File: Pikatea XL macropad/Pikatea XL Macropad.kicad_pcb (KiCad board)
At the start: 2 copper layers, 140.7 x 41 mm, 40 parts, among them J1 TC2030-CTX, J2 USB_B_Mini, J3 Conn_01x03_Male, J7 Conn_01x03_Male, SW1 SW_DPST, SW2 Rotary_Encoder_Switch, SW3 Rotary_Encoder_Switch, U1 ATMEGA32U4-EP, X1 16MHz

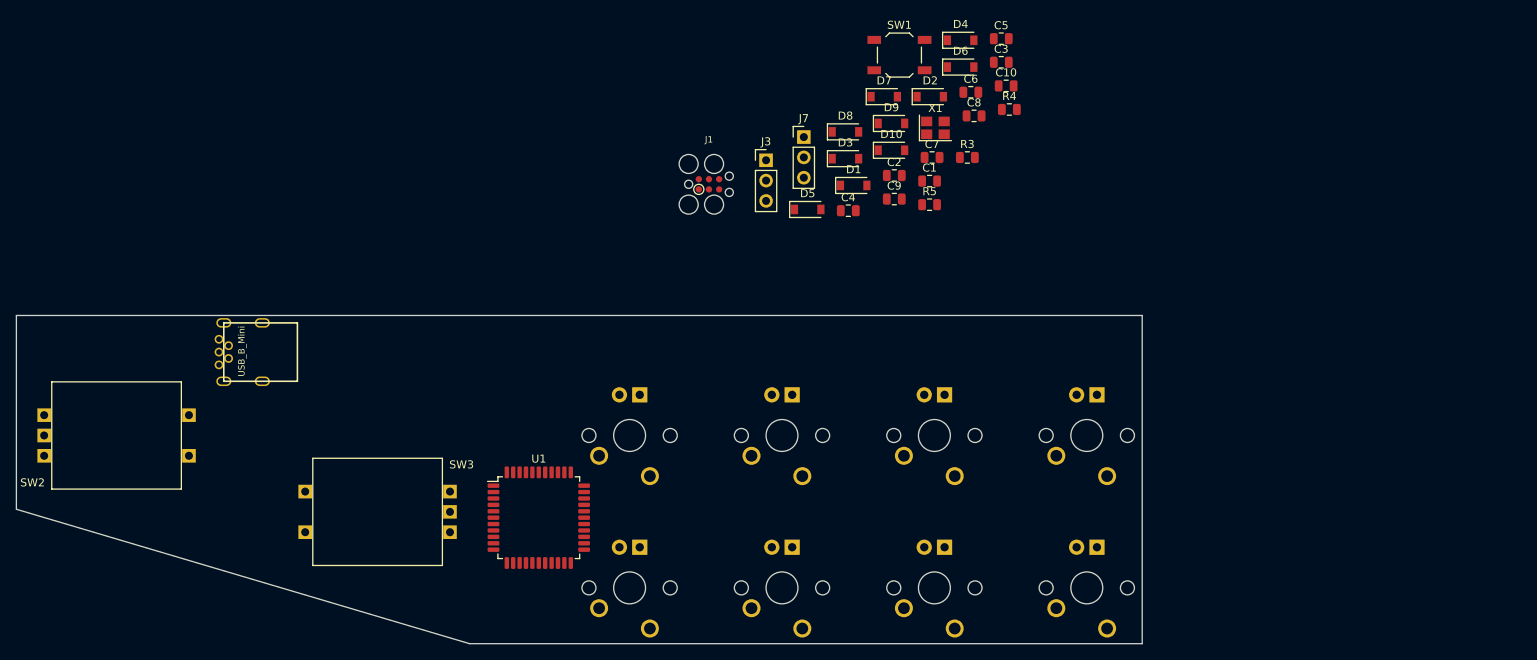
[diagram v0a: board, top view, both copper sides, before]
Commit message: add xl macropad pcb
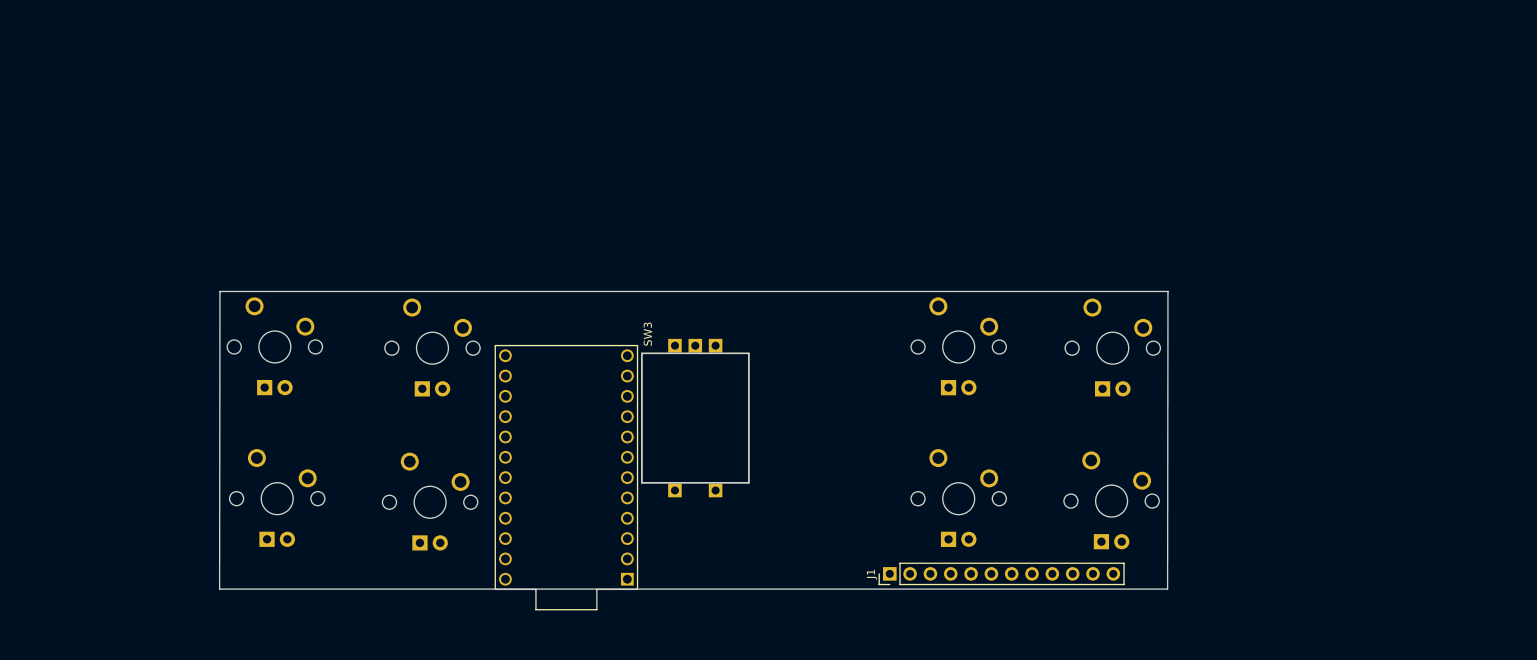
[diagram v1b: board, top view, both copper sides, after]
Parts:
- removed C1, C10, C2, C3, C4, C5: 0u1, Capacitor_SMD:C_0805_2012Metric
- removed C6: 4u7, Capacitor_SMD:C_0805_2012Metric
- removed C7, C8: 22p, Capacitor_SMD:C_0805_2012Metric
- removed C9: 1u, Capacitor_SMD:C_0805_2012Metric
- removed D1, D10, D2, D3, D4, D5, D6, D7, D8, D9: 1N4148W, Diode_SMD:D_SOD-123
- removed J2: USB_B_Mini, usb_mini:USB-Mini-B_ LCSC-C46398
- removed J3, J7: Conn_01x03_Male, Connector_PinHeader_2.54mm:PinHeader_1x03_P2.54mm_Vertical
- removed R3: 10K, Resistor_SMD:R_0805_2012Metric
- removed R4, R5: 22, Resistor_SMD:R_0805_2012Metric
- removed SW1: SW_DPST, Button_Switch_SMD:SW_SPST_TL3342
- removed SW2: Rotary_Encoder_Switch, Pikatea Macropad Encoder Side Mount:Encoder-BI_EN11_HSM0E
- removed X1: 16MHz, Crystal:Crystal_SMD_SeikoEpson_FA238-4Pin_3.2x2.5mm
- J1: value TC2030-CTX -> Conn_01x12_Female; footprint TC2030-CTX:TC2030-IDC -> Connector_PinHeader_2.54mm:PinHeader_1x12_P2.54mm_Vertical
- U1: value ATMEGA32U4-EP -> ProMicro; footprint Package_QFP:LQFP-44_10x10mm_P0.8mm -> promicro:ProMicro
- moved J1 53.7 mm to (132.5, 117.3), turned to 90 degrees
- moved MX1 45.7 mm to (55.7, 88.9), turned to 180 degrees
- moved MX5 45.4 mm to (56.0, 107.9), turned to 180 degrees
- moved MX6 45.3 mm to (75.1, 108.3), turned to 180 degrees
- moved MX2 45.0 mm to (75.4, 89.1), turned to 180 degrees
- moved SW3 41.4 mm to (108.2, 97.8), turned to 270 degrees
- moved MX7 11.6 mm to (141.1, 107.9), turned to 180 degrees
- moved MX3 11.5 mm to (141.1, 88.9), turned to 180 degrees
- moved MX4 11.4 mm to (160.4, 89.1), turned to 180 degrees
- moved MX8 11.3 mm to (160.2, 108.2), turned to 180 degrees
- moved U1 7.16 mm to (92.1, 104.0), turned to 90 degrees
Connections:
- J1 pad 1: VBUS -> (no net)
- J1 pad 2: /MOSI -> (no net)
- J1 pad 3: /RESET -> (no net)
- J1 pad 4: /SCK -> (no net)
- J1 pad 5: GND -> (no net)
- J1 pad 6: /MISO -> (no net)
- MX1 pad 3: Net-(MX1-Pad3) -> (no net)
- MX1 pad 4: Net-(MX1-Pad4) -> (no net)
- MX2 pad 3: Net-(MX2-Pad3) -> (no net)
- MX2 pad 4: Net-(MX2-Pad4) -> (no net)
- MX3 pad 3: Net-(MX3-Pad3) -> (no net)
- MX3 pad 4: Net-(MX3-Pad4) -> (no net)
- MX4 pad 3: Net-(MX4-Pad3) -> (no net)
- MX4 pad 4: Net-(MX4-Pad4) -> (no net)
- MX5 pad 3: Net-(MX5-Pad3) -> (no net)
- MX5 pad 4: Net-(MX5-Pad4) -> (no net)
- MX6 pad 3: Net-(MX6-Pad3) -> (no net)
- MX6 pad 4: Net-(MX6-Pad4) -> (no net)
- MX7 pad 3: Net-(MX7-Pad3) -> (no net)
- MX7 pad 4: Net-(MX7-Pad4) -> (no net)
- MX8 pad 3: Net-(MX8-Pad3) -> (no net)
- MX8 pad 4: Net-(MX8-Pad4) -> (no net)
- SW3 pad A: /D6 -> (no net)
- SW3 pad B: /D5 -> (no net)
- SW3 pad C: GND -> (no net)
- SW3 pad S2: /D2 -> (no net)
- U1 pad 1: /D7 -> (no net)
- U1 pad 10: /MOSI -> (no net)
- U1 pad 11: /MISO -> (no net)
- U1 pad 12: /D11 -> (no net)
- U1 pad 13: /RESET -> (no net)
- U1 pad 14: VBUS -> (no net)
- U1 pad 15: GND -> (no net)
- U1 pad 16: Net-(C8-Pad1) -> (no net)
- U1 pad 17: Net-(C7-Pad1) -> (no net)
- U1 pad 18: /D3 -> (no net)
- U1 pad 19: /D2 -> (no net)
- U1 pad 2: VBUS -> (no net)
- U1 pad 20: /D0 -> (no net)
- U1 pad 21: /D1 -> (no net)
- U1 pad 22: Net-(U1-Pad22) -> (no net)
- U1 pad 23: GND -> (no net)
- U1 pad 24: VBUS -> (no net)
- U1 pad 3: Net-(R5-Pad2) -> (no net)
- U1 pad 4: Net-(R4-Pad2) -> (no net)
- U1 pad 5: GND -> (no net)
- U1 pad 6: Net-(C9-Pad1) -> (no net)
- U1 pad 7: VBUS -> (no net)
- U1 pad 8: Net-(U1-Pad8) -> (no net)
- U1 pad 9: /SCK -> (no net)
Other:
- board size 140.7 x 41 mm -> 118.6 x 37.2 mm

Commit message: updates to XL macropad
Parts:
- added D1: 1N4148W, keyboard_parts:D_axial, F.Cu at (190.9, 90.6)
- added D2: 1N4148W, keyboard_parts:D_axial, F.Cu at (191.0, 105.0)
- added D3: 1N4148W, keyboard_parts:D_axial, F.Cu at (188.3, 90.6)
- added D4: 1N4148W, keyboard_parts:D_axial, F.Cu at (188.3, 105.0)
- added D5: 1N4148W, keyboard_parts:D_axial, F.Cu at (105.9, 92.5)
- added D6: 1N4148W, keyboard_parts:D_axial, F.Cu at (105.9, 105.0)
- added D7: 1N4148W, keyboard_parts:D_axial, F.Cu at (103.2, 92.5)
- added D8: 1N4148W, keyboard_parts:D_axial, F.Cu at (103.2, 105.0)
- added D9: 1N4148W, keyboard_parts:D_axial, F.Cu at (137.1, 92.5)
- moved MX1 144.7 mm to (199.2, 107.4), turned to 0 degrees
- moved MX5 144.5 mm to (199.2, 88.3), turned to 0 degrees
- moved MX6 106.9 mm to (180.1, 88.3), turned to 0 degrees
- moved MX2 106.3 mm to (180.1, 107.4), turned to 0 degrees
- moved U1 72.8 mm to (163.6, 90.4), turned to 270 degrees
- moved MX8 68.2 mm to (95.1, 88.3), turned to 0 degrees
- moved MX4 67.9 mm to (95.1, 107.4), turned to 0 degrees
- moved J1 41.5 mm to (122.1, 77.2), turned to 270 degrees
- moved SW3 38.9 mm to (147.1, 98.6), turned to 90 degrees
- moved MX7 33.4 mm to (114.1, 88.3), turned to 0 degrees
- moved MX3 32.7 mm to (114.1, 107.4), turned to 0 degrees
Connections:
- J1 pad 1: (no net) -> /A10
- J1 pad 10: (no net) -> /A3
- J1 pad 11: (no net) -> /A0
- J1 pad 12: (no net) -> /A4
- J1 pad 2: (no net) -> Net-(J1-Pad2)
- J1 pad 3: (no net) -> GND
- J1 pad 4: (no net) -> GND
- J1 pad 5: (no net) -> Net-(J1-Pad5)
- J1 pad 6: (no net) -> /B
- J1 pad 7: (no net) -> /A
- J1 pad 8: (no net) -> /D7
- J1 pad 9: (no net) -> /D9
- MX1 pad 3: (no net) -> Net-(MX1-Pad3)
- MX1 pad 4: (no net) -> Net-(MX1-Pad4)
- MX2 pad 3: (no net) -> Net-(MX2-Pad3)
- MX2 pad 4: (no net) -> Net-(MX2-Pad4)
- MX3 pad 3: (no net) -> Net-(MX3-Pad3)
- MX3 pad 4: (no net) -> Net-(MX3-Pad4)
- MX4 pad 3: (no net) -> Net-(MX4-Pad3)
- MX4 pad 4: (no net) -> Net-(MX4-Pad4)
- MX5 pad 3: (no net) -> Net-(MX5-Pad3)
- MX5 pad 4: (no net) -> Net-(MX5-Pad4)
- MX6 pad 3: (no net) -> Net-(MX6-Pad3)
- MX6 pad 4: (no net) -> Net-(MX6-Pad4)
- MX7 pad 3: (no net) -> Net-(MX7-Pad3)
- MX7 pad 4: (no net) -> Net-(MX7-Pad4)
- MX8 pad 3: (no net) -> Net-(MX8-Pad3)
- MX8 pad 4: (no net) -> Net-(MX8-Pad4)
- SW3 pad A: (no net) -> /A
- SW3 pad B: (no net) -> /B
- SW3 pad C: (no net) -> GND
- SW3 pad S2: (no net) -> /A10
- U1 pad 1: (no net) -> /A10
- U1 pad 10: (no net) -> /A3
- U1 pad 11: (no net) -> /A0
- U1 pad 12: (no net) -> /A4
- U1 pad 13: (no net) -> Net-(U1-Pad13)
- U1 pad 14: (no net) -> Net-(U1-Pad14)
- U1 pad 15: (no net) -> Net-(U1-Pad15)
- U1 pad 16: (no net) -> Net-(U1-Pad16)
- U1 pad 17: (no net) -> Net-(U1-Pad17)
- U1 pad 18: (no net) -> Net-(U1-Pad18)
- U1 pad 19: (no net) -> Net-(U1-Pad19)
- U1 pad 2: (no net) -> Net-(J1-Pad2)
- U1 pad 20: (no net) -> Net-(U1-Pad20)
- U1 pad 21: (no net) -> Net-(U1-Pad21)
- U1 pad 22: (no net) -> Net-(U1-Pad22)
- U1 pad 23: (no net) -> Net-(U1-Pad23)
- U1 pad 24: (no net) -> Net-(U1-Pad24)
- U1 pad 3: (no net) -> GND
- U1 pad 4: (no net) -> GND
- U1 pad 5: (no net) -> Net-(J1-Pad5)
- U1 pad 6: (no net) -> /B
- U1 pad 7: (no net) -> /A
- U1 pad 8: (no net) -> /D7
- U1 pad 9: (no net) -> /D9
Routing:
- net /D9: track 0.00 -> 190.4 mm, vias 0 -> 1
- net /A0: track 0.00 -> 164.3 mm, vias 0 -> 2
- net /D7: track 0.00 -> 146.3 mm, vias 0 -> 1
- net /A3: track 0.00 -> 120.7 mm, vias 0 -> 1
- net /A4: track 0.00 -> 108.8 mm
- net /B: track 0.00 -> 90.9 mm
- net /A: track 0.00 -> 89.0 mm
- net /A10: track 0.00 -> 52.1 mm, vias 0 -> 1
- net Net-(J1-Pad5): track 0.00 -> 50.9 mm
- net Net-(J1-Pad2): track 0.00 -> 38.0 mm
- net GND: track 0.00 -> 36.6 mm, vias 0 -> 42
- net /D8: track 0.00 -> 19.0 mm
- net Net-(D6-Pad1): track 0.00 -> 13.7 mm
- net Net-(D1-Pad1): track 0.00 -> 13.6 mm
- net Net-(D2-Pad1): track 0.00 -> 13.1 mm
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- added copper zone on B.Cu, net GND
- added copper zone on F.Cu, net GND
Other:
- board size 118.6 x 37.2 mm -> 118.3 x 40.8 mm
- board text added: "!print Beep Beep"
- board text added: "Pikatea Macropad XL"

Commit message: update auto save
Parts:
- MX1, MX2, MX3, MX4, MX5, MX6, MX7, MX8: footprint MX_Only:MXOnly-1U -> MX_Only:MXOnly-1U-NoLED
- turned D1 to 90 degrees
- turned D2 to 270 degrees
- turned D3 to 90 degrees
- turned D4 to 270 degrees
- turned D5 to 270 degrees
- turned D6 to 270 degrees
- turned D7 to 270 degrees
- turned D8 to 270 degrees
- turned D9 to 270 degrees
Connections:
- D1 pad 1: Net-(D1-Pad1) -> /A3
- D1 pad 2: /A3 -> Net-(D1-Pad2)
- D2 pad 1: Net-(D2-Pad1) -> /A0
- D2 pad 2: /A0 -> Net-(D2-Pad2)
- D3 pad 1: Net-(D3-Pad1) -> /A3
- D3 pad 2: /A3 -> Net-(D3-Pad2)
- D4 pad 1: Net-(D4-Pad1) -> /A0
- D4 pad 2: /A0 -> Net-(D4-Pad2)
- D5 pad 1: Net-(D5-Pad1) -> /A3
- D5 pad 2: /A3 -> Net-(D5-Pad2)
- D6 pad 1: Net-(D6-Pad1) -> /A0
- D6 pad 2: /A0 -> Net-(D6-Pad2)
- D7 pad 1: Net-(D7-Pad1) -> /A3
- D7 pad 2: /A3 -> Net-(D7-Pad2)
- D8 pad 1: Net-(D8-Pad1) -> /A0
- D8 pad 2: /A0 -> Net-(D8-Pad2)
- D9 pad 1: Net-(D9-Pad1) -> /A3
- D9 pad 2: /A3 -> Net-(D9-Pad2)
- J1 pad 5: Net-(J1-Pad5) -> /D8
- MX1 pad 2: Net-(D2-Pad1) -> Net-(D2-Pad2)
- MX2 pad 2: Net-(D4-Pad1) -> Net-(D4-Pad2)
- MX3 pad 2: Net-(D6-Pad1) -> Net-(D6-Pad2)
- MX4 pad 2: Net-(D8-Pad1) -> Net-(D8-Pad2)
- MX5 pad 2: Net-(D1-Pad1) -> Net-(D1-Pad2)
- MX6 pad 2: Net-(D3-Pad1) -> Net-(D3-Pad2)
- MX7 pad 2: Net-(D5-Pad1) -> Net-(D5-Pad2)
- MX8 pad 2: Net-(D7-Pad1) -> Net-(D7-Pad2)
- SW3 pad S1: Net-(D9-Pad1) -> Net-(D9-Pad2)
- U1 pad 13: Net-(U1-Pad13) -> (no net)
- U1 pad 14: Net-(U1-Pad14) -> (no net)
- U1 pad 15: Net-(U1-Pad15) -> (no net)
- U1 pad 16: Net-(U1-Pad16) -> (no net)
- U1 pad 17: Net-(U1-Pad17) -> (no net)
- U1 pad 18: Net-(U1-Pad18) -> (no net)
- U1 pad 19: Net-(U1-Pad19) -> (no net)
- U1 pad 20: Net-(U1-Pad20) -> (no net)
- U1 pad 21: Net-(U1-Pad21) -> (no net)
- U1 pad 22: Net-(U1-Pad22) -> (no net)
- U1 pad 23: Net-(U1-Pad23) -> (no net)
- U1 pad 24: Net-(U1-Pad24) -> (no net)
- U1 pad 5: Net-(J1-Pad5) -> /D8
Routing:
- net /D8: track 19.0 -> 85.0 mm, vias 0 -> 1
- net Net-(J1-Pad5): track 50.9 -> 0.00 mm
- net Net-(D6-Pad2): track 0.00 -> 13.7 mm
- net Net-(D6-Pad1): track 13.7 -> 0.00 mm
- net Net-(D1-Pad2): track 0.00 -> 13.6 mm
- net Net-(D1-Pad1): track 13.6 -> 0.00 mm
- net Net-(D2-Pad2): track 0.00 -> 13.1 mm
- net Net-(D2-Pad1): track 13.1 -> 0.00 mm
- net Net-(D9-Pad2): track 0.00 -> 13.0 mm
- net Net-(D9-Pad1): track 13.0 -> 0.00 mm
- net Net-(D5-Pad2): track 0.00 -> 12.0 mm
- net Net-(D5-Pad1): track 12.0 -> 0.00 mm
- net Net-(D3-Pad2): track 0.00 -> 11.0 mm
- net Net-(D3-Pad1): track 11.0 -> 0.00 mm
- net Net-(D4-Pad2): track 0.00 -> 8.18 mm
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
